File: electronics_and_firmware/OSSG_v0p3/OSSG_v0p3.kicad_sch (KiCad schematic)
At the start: 77 parts, among them IC1 DW01A, J1 USB_B_Micro, J2 External PDM Mic Input, Q1 FS8205A, Q2 Q_NPN_BEC, Q3 Q_NPN_BEC, SW1 SW_SPST, U1 ESP32-PICO-D4, U2 TP4056, U3 XC6222B331MRG, U4 FT232RQ, U5 APX803L-29SA-7, U6 MP23DB01HPTR

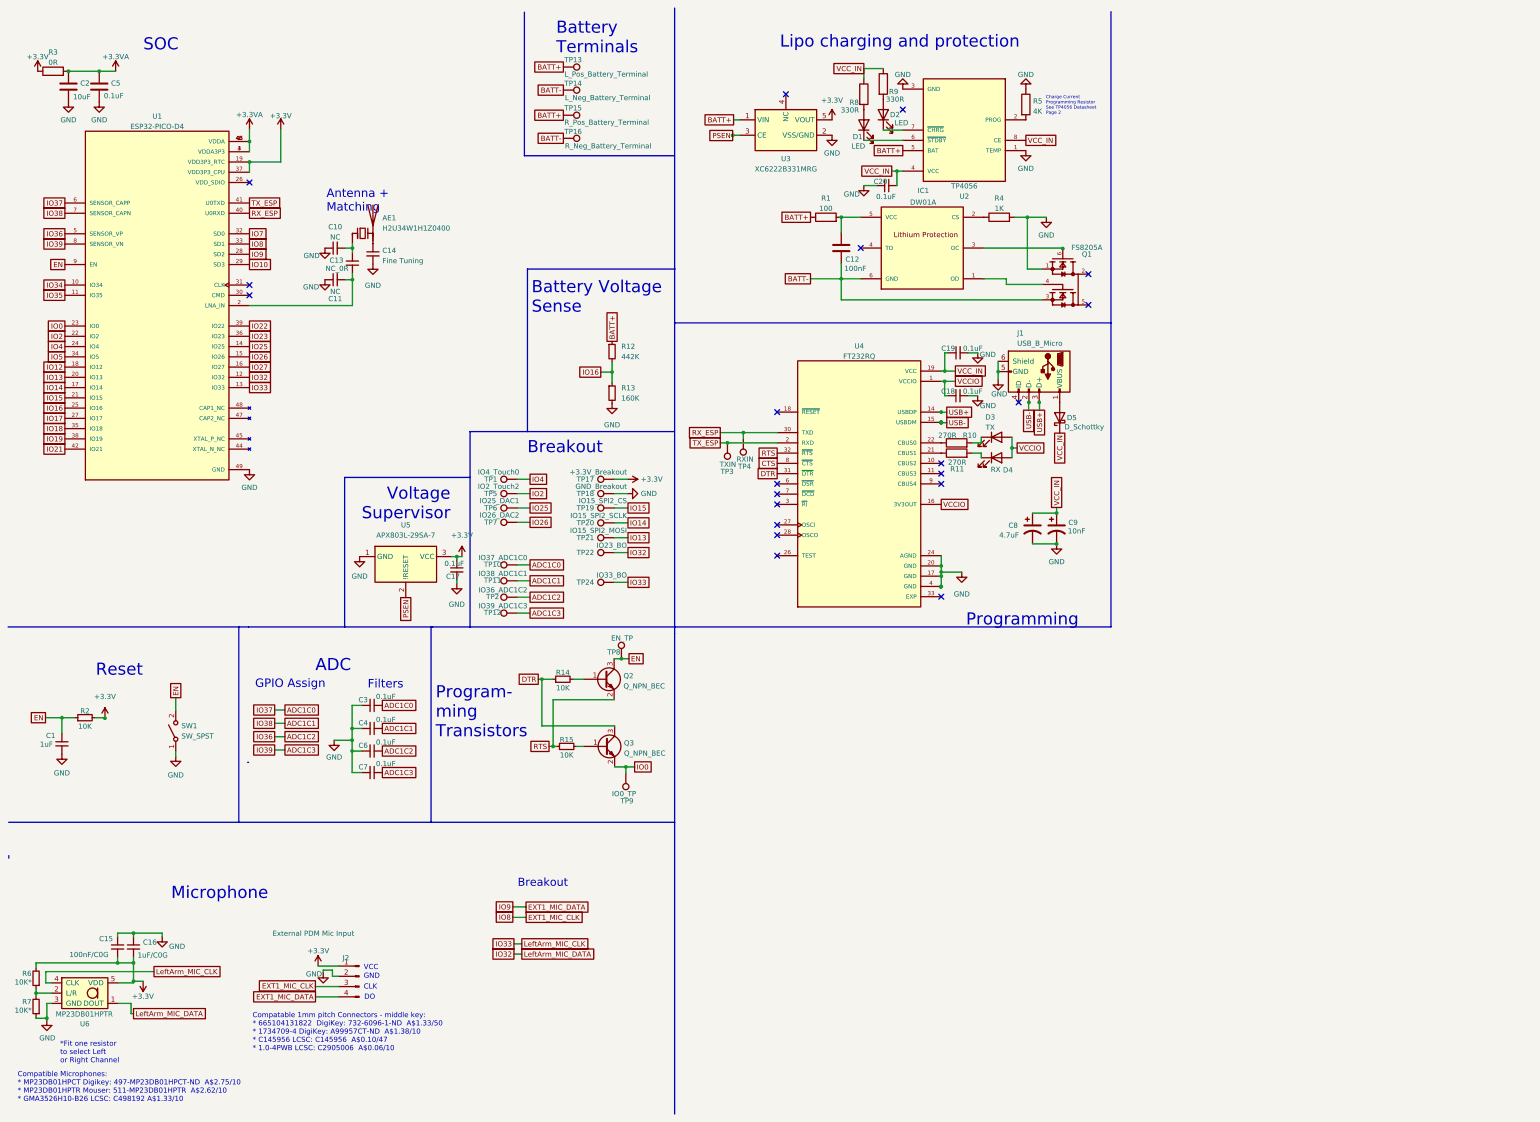
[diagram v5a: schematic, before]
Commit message: switch from FT232 to CH99102F in schematic
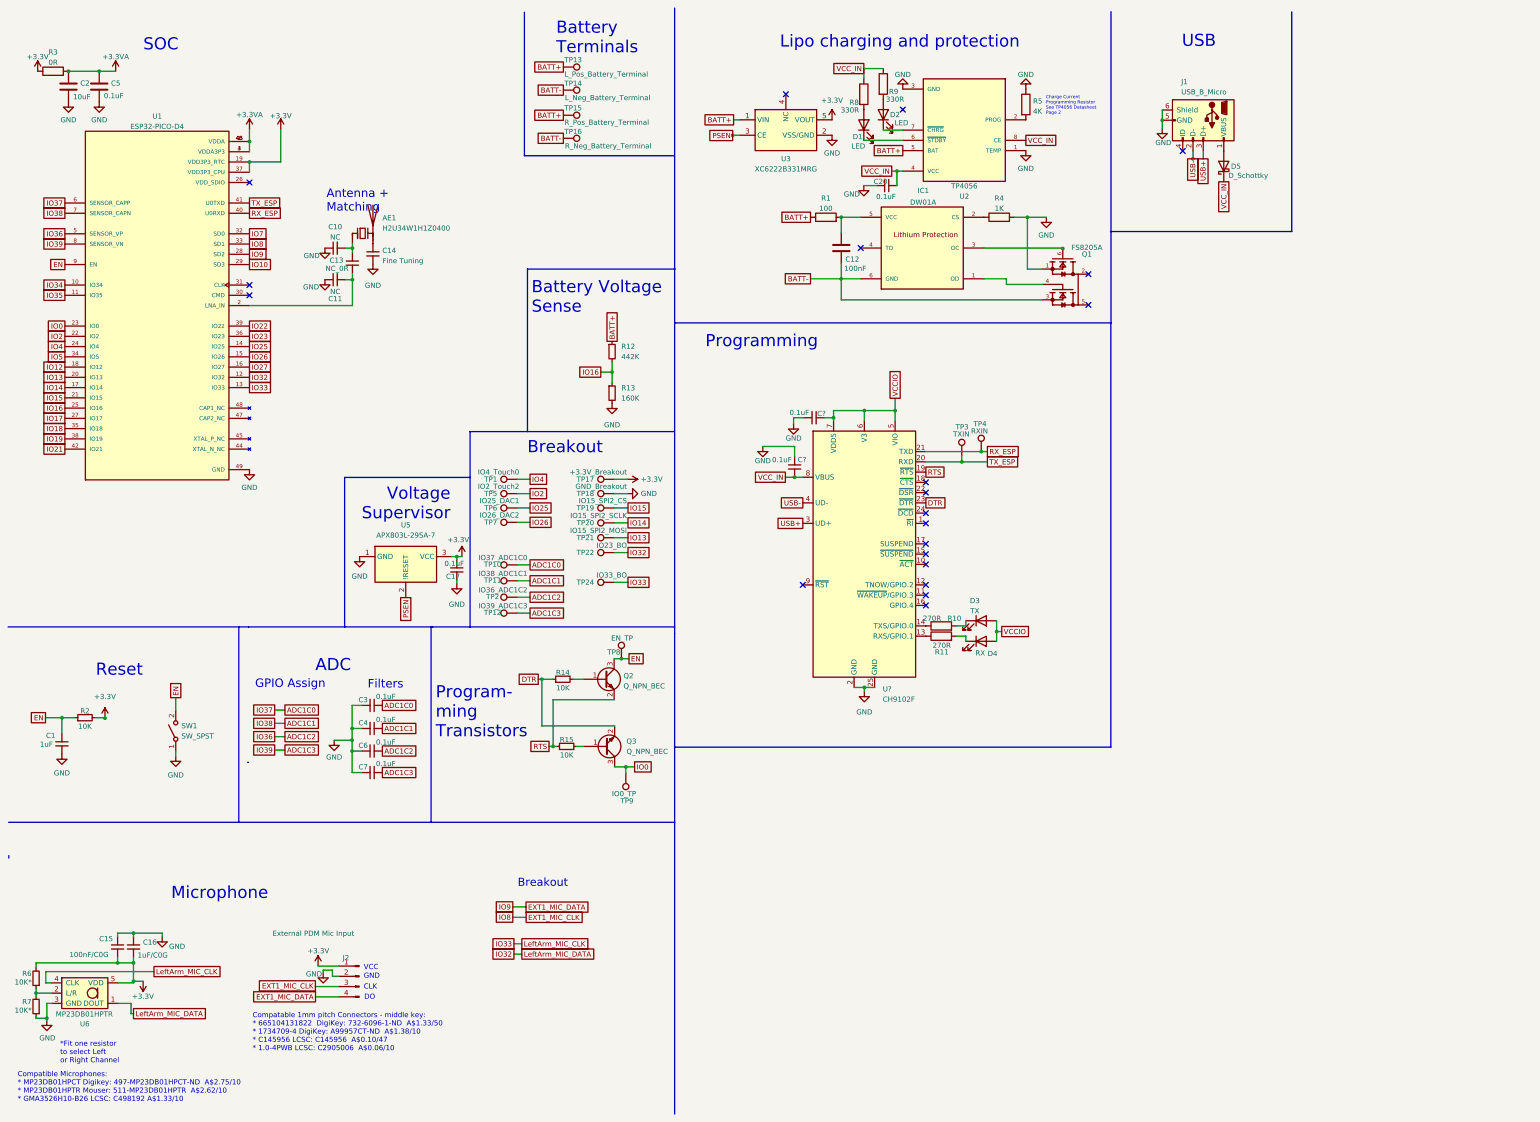
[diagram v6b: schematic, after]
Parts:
- removed C18, C19: 0.1uF, Capacitor_SMD:C_0402_1005Metric, symbol Device:C_Small
- removed C8: 4.7uF, Capacitor_SMD:C_0402_1005Metric, symbol Device:C_Polarized_US
- removed C9: 10nF, Capacitor_SMD:C_0402_1005Metric, symbol Device:C_Polarized_US
- removed U4: FT232RQ, OpenSourceSmartGlasses:QFN32_5mmx5mm_smallEP, symbol FT232RQ:FT232RQ
- added C? (x2): 0.1uF, Capacitor_SMD:C_0402_1005Metric, symbol Device:C_Small
- added U?: CH9102F, Package_DFN_QFN:QFN-24-1EP_4x4mm_P0.5mm_EP2.6x2.6mm, symbol wch-usb-uart:CH9102F
- SW1: footprint Button_Switch_SMD:SW_SPST_B3U-3100P-B -> Button_Switch_SMD:SW_SPST_B3U-3000P-B; LCSCLink (none) -> https://lcsc.com/product-detail/Tactile-Switches_Omron-Elec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; MPN_LCSC (none) -> C306884; Price_LCSSC (none) -> 0.7718
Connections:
- net DTR: now also Q3.2 (E), U?.23 (~{DTR}); no longer Q3.3 (C)
- net GND: now also C?.1, C?.2, U?.2 (GND), U?.25 (GND)
- net IO0: now also Q3.3 (C); no longer Q3.2 (E)
- net RTS: now also U?.19 (~{RTS})
- net RX_ESP: now also U?.21 (TXD)
- net TX_ESP: now also U?.20 (RXD)
- net USB+: now also U?.3 (UD+)
- net USB-: now also U?.4 (UD-)
- net VCCIO: now also C?.1, U?.5 (VIO), U?.6 (V3), U?.7 (VDD5)
- net VCC_IN: now also C?.2, U?.8 (VBUS)
- net at R11.1: now also U?.13 (RXS/GPIO.1)
- net at R10.1: now also U?.14 (TXS/GPIO.0)
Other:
- note added: "USB"
- moved on the sheet: D3, D4, D5, J1, R10, R11, TP3, TP4

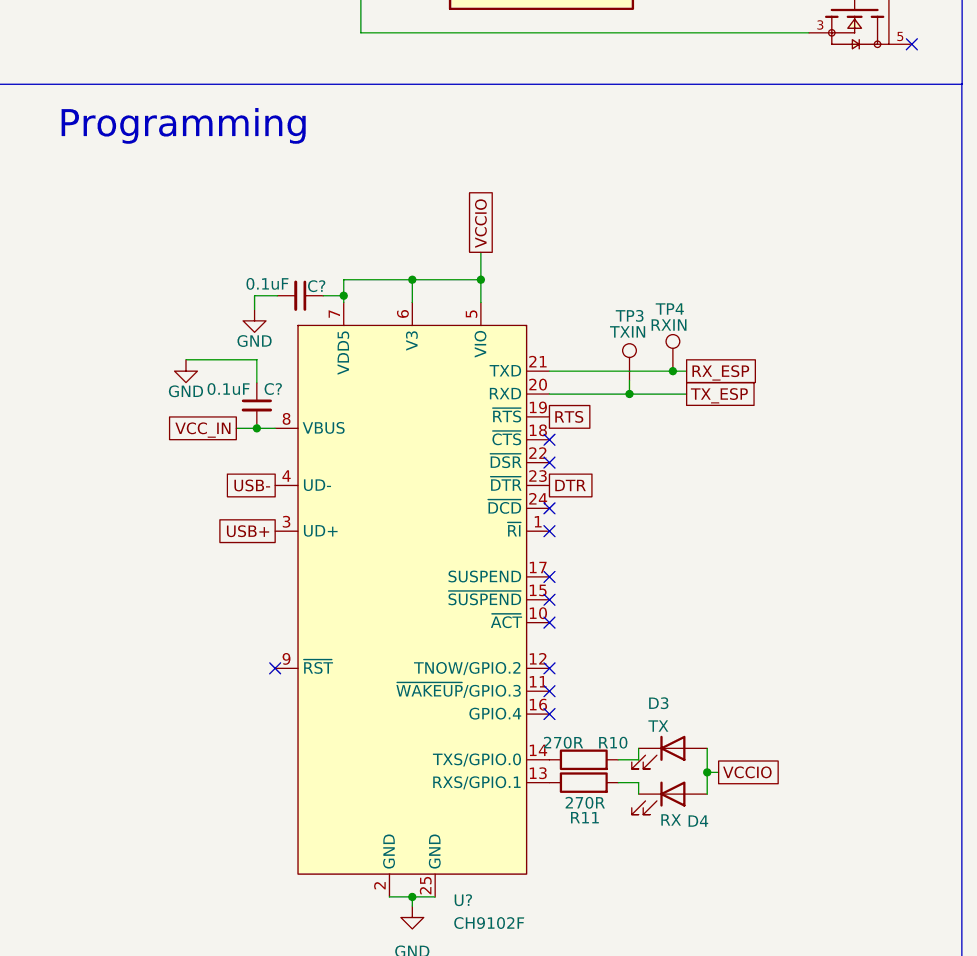
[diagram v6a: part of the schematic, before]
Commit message: attempt to fix CH9102F programmer circuit
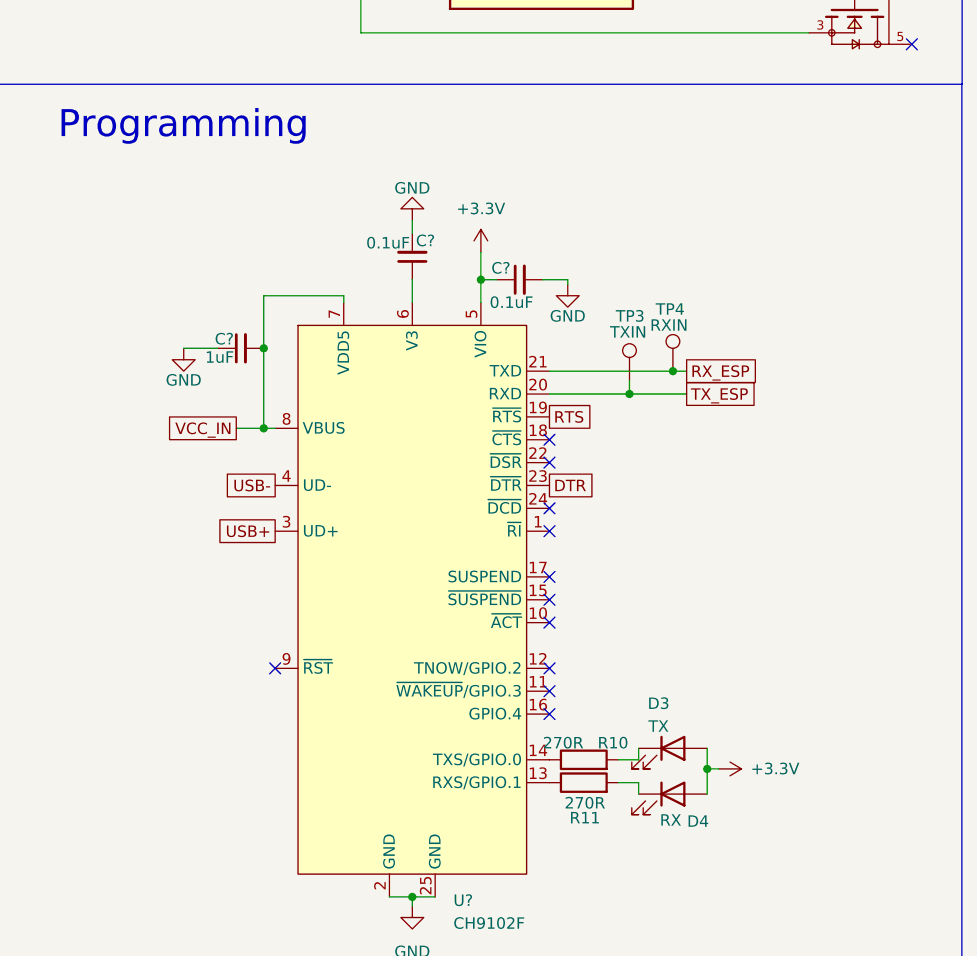
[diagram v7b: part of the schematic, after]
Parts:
- removed C?: 0.1uF, Capacitor_SMD:C_0402_1005Metric, symbol Device:C_Small
- added C?: 1uF, Capacitor_SMD:C_0402_1005Metric, symbol Device:C_Small
- added C?: 0.1uF, Capacitor_SMD:C_0402_1005Metric, symbol Device:C_Small
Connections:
- net +3V3: now also D3.2 (A), D4.2 (A), U?.5 (VIO), C?.1
- net GND: now also C?.1, C?.2
- net VCC_IN: now also U?.7 (VDD5), C?.2
- removed net VCCIO: C?.1, D3.2 (A), D4.2 (A), U?.5 (VIO), U?.6 (V3), U?.7 (VDD5)
- new net: C?.1, U?.6 (V3)
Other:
- moved on the sheet: C?
